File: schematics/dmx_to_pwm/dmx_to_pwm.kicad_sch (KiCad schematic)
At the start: 39 parts, among them J2 DMX-IN, J3 DMX-OUT, Q1 BS170, Q10 BS170, Q11 BS170, Q12 BS170, Q2 BS170, Q3 BS170, Q4 BS170, Q5 BS170, Q6 BS170, Q7 BS170, Q8 BS170, Q9 BS170, U1 SN75176AP, U2 6N137, U3 6N137, U4 SN75176AP

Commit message: updated some components
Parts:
- removed Q1, Q10, Q11, Q12, Q2, Q3, Q4, Q5, Q6, Q7, Q8, Q9: BS170, Package_TO_SOT_THT:TO-92_Inline, symbol Transistor_FET:BS170
- added C3: 10uF, symbol Device:C_Polarized
- added C4: 330nF, symbol Device:C
- added C5, C6: 100nF, symbol Device:C
- added D1, D2: 1N4148, Diode_THT:D_DO-35_SOD27_P7.62mm_Horizontal, symbol Diode:1N4148
- added J4: PJ-031D, PJ031D, symbol PJ-031D:PJ-031D
- added SW2: SW_SPDT, Button_Switch_THT:SW_Slide-03_Wuerth-WS-SLTV_10x2.5x6.4_P2.54mm, symbol Switch:SW_Wuerth_450301014042
- added SW3: SW_Push_DPDT, symbol Switch:SW_Push_DPDT
- added U5: LM7812_TO220, Package_TO_SOT_THT:TO-220-3_Vertical, symbol Regulator_Linear:LM7812_TO220
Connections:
- net GND is gone; now on net DRV1-: A1.29 (GND), A1.4 (GND), C1.2, C2.2, J2.7, J2.8, J3.7, J3.8, R17.2, U1.2 (~{RE}), U1.3 (DE), U1.4 (D), U1.5 (GND), U2.3 (C), U2.5 (GND), U3.3 (C), U3.5 (GND), U4.5 (GND)
- net DATA10: now also R10.1; no longer R4.1
- net DATA11: now also R11.1; no longer R5.1
- net DATA12: now also R12.1; no longer R6.1
- net DATA2: now also R1.1; no longer R8.1
- net DATA3: now also R2.1; no longer R9.1
- net DATA4: now also R3.1; no longer R10.1
- net DATA5: now also R4.1; no longer R11.1
- net DATA6: now also R5.1; no longer R12.1
- net DATA7: now also R6.1; no longer R1.1
- net DATA8: now also R8.1; no longer R2.1
- net DATA9: now also R9.1; no longer R3.1
- net DRV1+: now also R7.2; no longer C1.1, C2.1, R14.1, R16.1, R19.2, U1.8 (VCC), U2.8 (VCC), U3.7 (EN), U3.8 (VCC), U4.2 (~{RE}), U4.3 (DE), U4.8 (VCC)
- net DRV1-: now also C3.2, C4.2, C5.2, C6.1, J4.1, U5.2 (GND)
- net DRV3+: now reaches R2.2
- net DRV11+: now reaches R11.2
- net DRV4+: now reaches R3.2
- net DRV2+: now reaches R1.2
- net VIN: now reaches A1.30 (VIN)
- net VIN: now also C6.2, D1.1 (K), D2.1 (K), SW2.3 (A), SW3.4 (A)
- net DRV12+: now reaches R12.2
- net DRV5+: now reaches R4.2
- net DRV9+: now reaches R9.2
- net at J2.5: now also J2.6, SW3.2 (B)
- net DRV7+: now reaches R6.2
- net DRV10+: now reaches R10.2
- net DRV6+: now reaches R5.2
- net at J3.5: now also J3.6, SW3.5 (B)
- net DRV8+: now reaches R8.2
- new net: C3.1, J4.3
- new net: C4.1, U5.1 (VI)
- new net: C5.1, D2.2 (A), U5.3 (VO)
- new net: SW2.1 (B), SW3.1 (A)
- new net VCC: C1.1, C2.1, R14.1, R16.1, R19.2, U1.8 (VCC), U2.8 (VCC), U3.7 (EN), U3.8 (VCC), U4.2 (~{RE}), U4.3 (DE), U4.8 (VCC)
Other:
- note added: "POE ON/OFF"
- note added: "POE_IN ON/OFF"
- note added: "VOLTAGE REGULATOR ON/OFF"
- moved on the sheet: A1, C1, C2, R13, R14, R15, R16, R17, R19, R7, U1, U2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

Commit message: improved schematics
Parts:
- removed SW3: SW_Push_DPDT, symbol Switch:SW_Push_DPDT
- added SW1: SW_SPDT, Button_Switch_THT:SW_Slide-03_Wuerth-WS-SLTV_10x2.5x6.4_P2.54mm, symbol Switch:SW_Wuerth_450301014042
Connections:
- net VIN: now also SW1.3 (A)
- net at SW2.1 (B): now also J2.5, J2.6
- net at J3.5, J3.6: now also SW1.1 (B)
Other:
- note added: "POE_OUT ON/OFF"
- note removed: "POE ON/OFF"
- moved on the sheet: SW2
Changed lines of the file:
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@@
 	)
 	(junction
-		(at 46.99 48.26)
+		(at 157.48 33.02)
 		(diameter 0)
 		(color 0 0 0 0)
 	)
 	(junction
-		(at 157.48 33.02)
+		(at 46.99 48.26)
 		(diameter 0)
 		(color 0 0 0 0)
@@
 	(wire
 		(pts
-			(xy 46.99 52.07) (xy 46.99 48.26)
-		)
-		(stroke
-			(width 0)
-			(type default)
-		)
-	)
-	(wire
-		(pts
 			(xy 267.97 76.2) (xy 266.7 76.2)
 		)
@@
 	(wire
 		(pts
+			(xy 46.99 48.26) (xy 63.5 48.26)
+		)
+		(stroke
+			(width 0)
+			(type default)
+		)
+	)
+	(wire
+		(pts
 			(xy 104.14 44.45) (xy 104.14 38.1)
 		)
@@
 	(wire
 		(pts
-			(xy 57.15 49.53) (xy 63.5 49.53)
-		)
-		(stroke
-			(width 0)
-			(type default)
-		)
-	)
-	(wire
-		(pts
 			(xy 223.52 91.44) (xy 226.06 91.44)
 		)
@@
 		)
 	)
-	(text "POE ON/OFF"
+	(text "POE_OUT ON/OFF"
 		(exclude_from_sim no)
 		(at 52.07 68.072 0)
@@
 	(text "POE_IN ON/OFF"
 		(exclude_from_sim no)
-		(at 69.342 55.88 0)
+		(at 69.342 54.102 0)
 		(effects
 			(font
@@
 		)
 	)
-	(global_label "VIN"
-		(shape input)
-		(at 57.15 59.69 0)
-		(fields_autoplaced yes)
-		(effects
-			(font
-				(size 1.27 1.27)
-			)
-			(justify left)
-		)
-		(property "Intersheetrefs" "${INTERSHEET_REFS}"
-			(at 63.1591 59.69 0)
-			(effects
-				(font
-					(size 1.27 1.27)
-				)
-				(justify left)
-				(hide yes)
-			)
-		)
-	)
 	(global_label "DATA11"
 		(shape input)
@@
 		)
 	)
+	(global_label "VIN"
+		(shape input)
+		(at 57.15 59.69 0)
+		(fields_autoplaced yes)
+		(effects
+			(font
+				(size 1.27 1.27)
+			)
+			(justify left)
+		)
+		(property "Intersheetrefs" "${INTERSHEET_REFS}"
+			(at 63.1591 59.69 0)
+			(effects
+				(font
+					(size 1.27 1.27)
+				)
+				(justify left)
+				(hide yes)
+			)
+		)
+	)
 	(global_label "DRV6-"
 		(shape input)
@@
 	(global_label "VIN"
 		(shape input)
-		(at 73.66 46.99 0)
+		(at 73.66 45.72 0)
 		(fields_autoplaced yes)
 		(effects
@@
 		)
 		(property "Intersheetrefs" "${INTERSHEET_REFS}"
-			(at 79.6691 46.99 0)
+			(at 79.6691 45.72 0)
 			(effects
 				(font
@@
 	(symbol
 		(lib_id "Switch:SW_Wuerth_450301014042")
-		(at 68.58 49.53 0)
+		(at 68.58 48.26 0)
 		(unit 1)
 		(exclude_from_sim no)
@@
 		(fields_autoplaced yes)
 		(property "Reference" "SW2"
-			(at 68.58 40.64 0)
+			(at 68.58 39.37 0)
 			(effects
 				(font
@@
 		)
 		(property "Value" "SW_SPDT"
-			(at 68.58 43.18 0)
+			(at 68.58 41.91 0)
 			(effects
 				(font
@@
 		)
 		(property "Footprint" "Button_Switch_THT:SW_Slide-03_Wuerth-WS-SLTV_10x2.5x6.4_P2.54mm"
-			(at 68.58 59.69 0)
+			(at 68.58 58.42 0)
 			(effects
 				(font
@@
 		)
 		(property "Datasheet" "https://www.we-online.com/components/products/datasheet/450301014042.pdf"
-			(at 68.58 57.15 0)
+			(at 68.58 55.88 0)
 			(effects
 				(font
@@
 		)
 		(property "Description" "Switch slide, single pole double throw"
-			(at 68.58 49.53 0)
+			(at 68.58 48.26 0)
 			(effects
 				(font
@@
 	)
 	(symbol
+		(lib_id "Switch:SW_Wuerth_450301014042")
+		(at 52.07 62.23 0)
+		(unit 1)
+		(exclude_from_sim no)
+		(in_bom yes)
+		(on_board yes)
+		(dnp no)
+		(fields_autoplaced yes)
+		(property "Reference" "SW1"
+			(at 52.07 53.34 0)
+			(effects
+				(font
+					(size 1.27 1.27)
+				)
+			)
+		)
+		(property "Value" "SW_SPDT"
+			(at 52.07 55.88 0)
+			(effects
+				(font
+					(size 1.27 1.27)
+				)
+			)
+		)
+		(property "Footprint" "Button_Switch_THT:SW_Slide-03_Wuerth-WS-SLTV_10x2.5x6.4_P2.54mm"
+			(at 52.07 72.39 0)
+			(effects
+				(font
+					(size 1.27 1.27)
+				)
+				(hide yes)
+			)
+		)
+		(property "Datasheet" "https://www.we-online.com/components/products/datasheet/450301014042.pdf"
+			(at 52.07 69.85 0)
+			(effects
+				(font
+					(size 1.27 1.27)
+				)
+				(hide yes)
+			)
+		)
+		(property "Description" "Switch slide, single pole double throw"
+			(at 52.07 62.23 0)
+			(effects
+				(font
+					(size 1.27 1.27)
+				)
+				(hide yes)
+			)
+		)
+		(pin "1"
+		)
+		(pin "2"
+		)
+		(pin "3"
+		)
+		(instances
+			(project "dmx_to_pwm"
+				(path "/fe39f169-33b8-46fd-886b-c754b4eb741b"
+					(reference "SW1")
+					(unit 1)
+				)
+			)
+		)
+	)
+	(symbol
 		(lib_id "Device:R_US")
 		(at 219.71 24.13 90)
@@
 					(unit 1)
 				)
-			)
-		)
-	)
-	(symbol
-		(lib_id "Switch:SW_Push_DPDT")
-		(at 52.07 57.15 0)
-		(unit 1)
-		(exclude_from_sim no)
-		(in_bom yes)
-		(on_board yes)
-		(dnp no)
-		(property "Reference" "SW3"
-			(at 52.07 43.18 0)
-			(effects
-				(font
-					(size 1.27 1.27)
-				)
-			)
-		)
-		(property "Value" "SW_Push_DPDT"
-			(at 55.626 45.72 0)
-			(effects
-				(font
-					(size 1.27 1.27)
-				)
-			)
-		)
-		(property "Footprint" ""
-			(at 52.07 52.07 0)
-			(effects
-				(font
-					(size 1.27 1.27)
-				)
-				(hide yes)
-			)
-		)
-		(property "Datasheet" "~"
-			(at 52.07 52.07 0)
-			(effects
-				(font
-					(size 1.27 1.27)
-				)
-				(hide yes)
-			)
-		)
-		(property "Description" "Momentary Switch, dual pole double throw"
-			(at 52.07 57.15 0)
-			(effects
-				(font
-					(size 1.27 1.27)
-				)
-				(hide yes)
-			)
-		)
-		(pin "2"
-		)
-		(pin "1"
-		)
-		(pin "5"
-		)
-		(pin "3"
-		)
-		(pin "4"
-		)
-		(pin "6"
-		)
-		(instances
-			(project "dmx_to_pwm"
-				(path "/fe39f169-33b8-46fd-886b-c754b4eb741b"
-					(reference "SW3")
-					(unit 1)
-				)

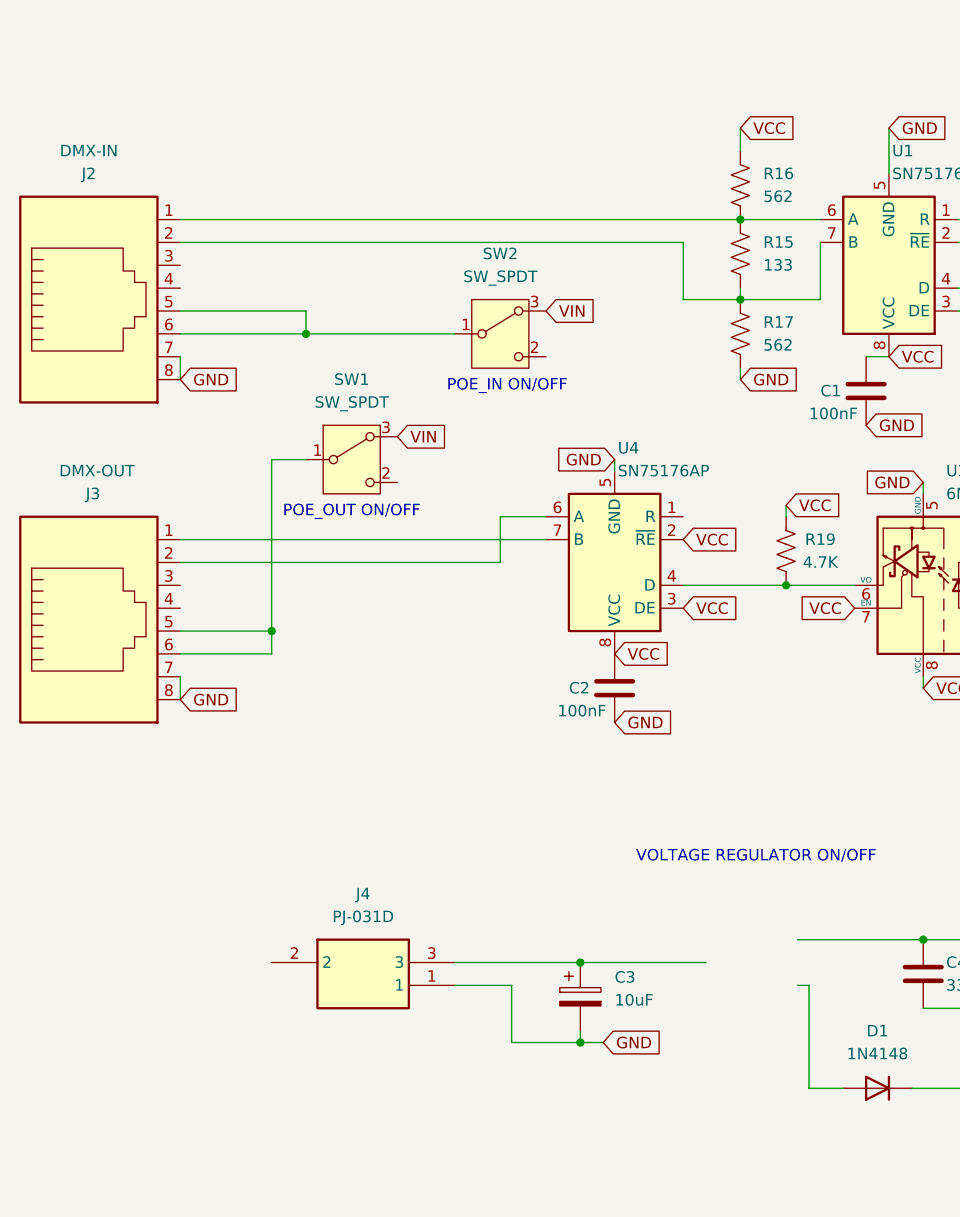
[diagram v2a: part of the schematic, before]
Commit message: #5 improved schematics
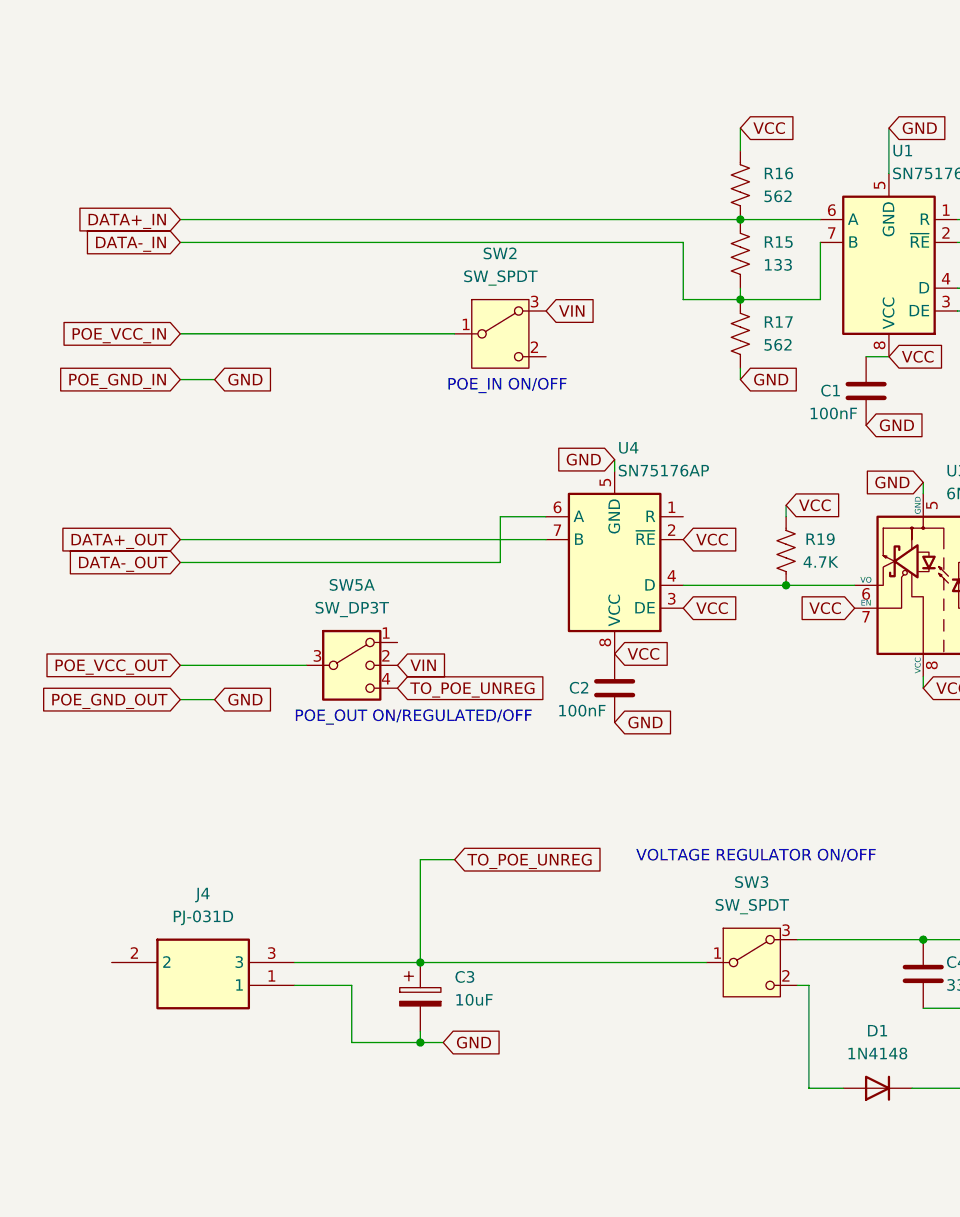
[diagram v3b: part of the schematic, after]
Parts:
- removed J2: DMX-IN, symbol Connector:RJ45
- removed J3: DMX-OUT, symbol Connector:RJ45
- removed SW1: SW_SPDT, Button_Switch_THT:SW_Slide-03_Wuerth-WS-SLTV_10x2.5x6.4_P2.54mm, symbol Switch:SW_Wuerth_450301014042
- added SW3: SW_SPDT, Button_Switch_THT:SW_Slide-03_Wuerth-WS-SLTV_10x2.5x6.4_P2.54mm, symbol Switch:SW_Wuerth_450301014042
- added SW5: SW_DP3T, symbol Switch:SW_DP3T
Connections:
- net VIN: now also SW5.2
- net TO_POE_UNREG: now reaches C3.1, J4.3
- net TO_POE_UNREG: now also SW3.1 (B), SW5.4
- net DATA+_IN: now reaches R15.1, R16.2, U1.6 (A)
- net DATA-_IN: now reaches R15.2, R17.1, U1.7 (B)
- net at C4.1, U5.1 (VI): now also SW3.3 (A)
- net at D1.2 (A): now also SW3.2 (C)
- net POE_VCC_IN: now reaches SW2.1 (B)
- net DATA+_OUT: now reaches U4.7 (B)
- net DATA-_OUT: now reaches U4.6 (A)
- new net POE_VCC_OUT: SW5.3
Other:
- note added: "POE_OUT ON/REGULATED/OFF"
- note removed: "POE_OUT ON/OFF"
- moved on the sheet: C3, J4

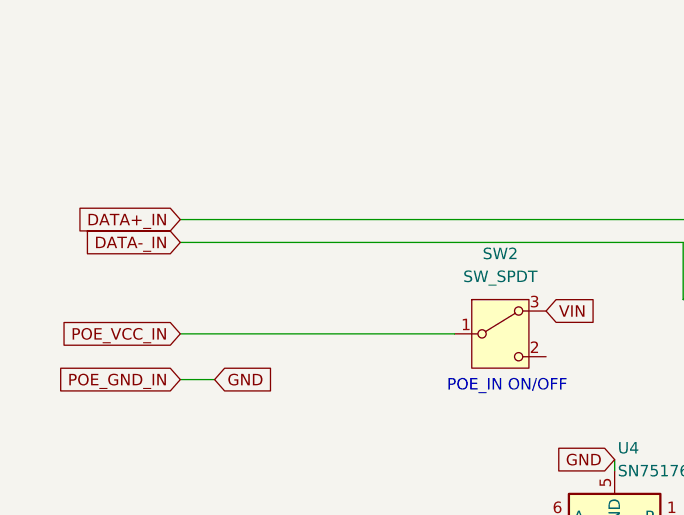
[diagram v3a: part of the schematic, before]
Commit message: added some prototype info to the schematics
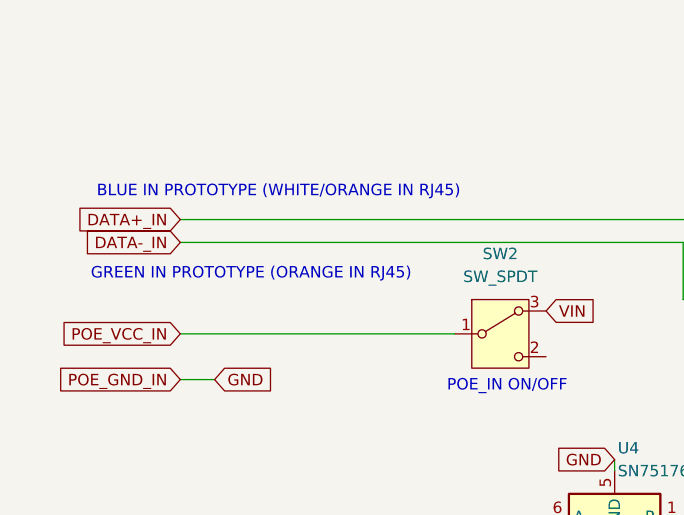
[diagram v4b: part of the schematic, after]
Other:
- note added: "BLUE IN PROTOTYPE (WHITE/ORANGE IN RJ45)"
- note added: "GREEN IN PROTOTYPE (ORANGE IN RJ45)"
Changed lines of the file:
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@@
+		)
+	)
+	(text "GREEN IN PROTOTYPE (ORANGE IN RJ45)"
+		(exclude_from_sim no)
+		(at 40.894 41.656 0)
+		(effects
+			(font
+				(size 1.27 1.27)
+			)
+		)
+	)
+	(text "BLUE IN PROTOTYPE (WHITE/ORANGE IN RJ45)"
+		(exclude_from_sim no)
+		(at 43.942 32.512 0)
+		(effects
+			(font
+				(size 1.27 1.27)
+			)
 		)
 	)

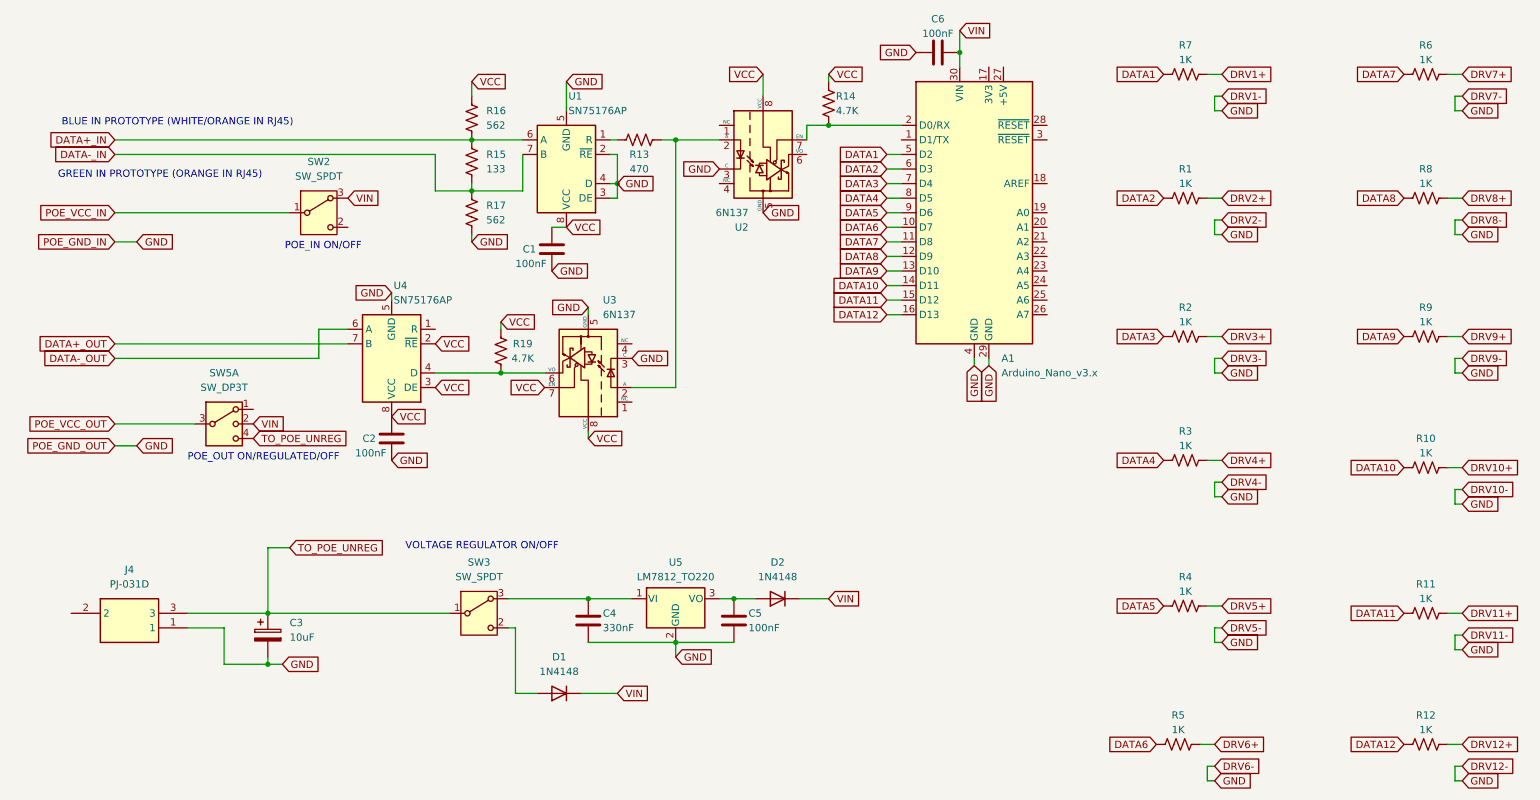
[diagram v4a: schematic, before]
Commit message: updated schematics, added laser module blender file
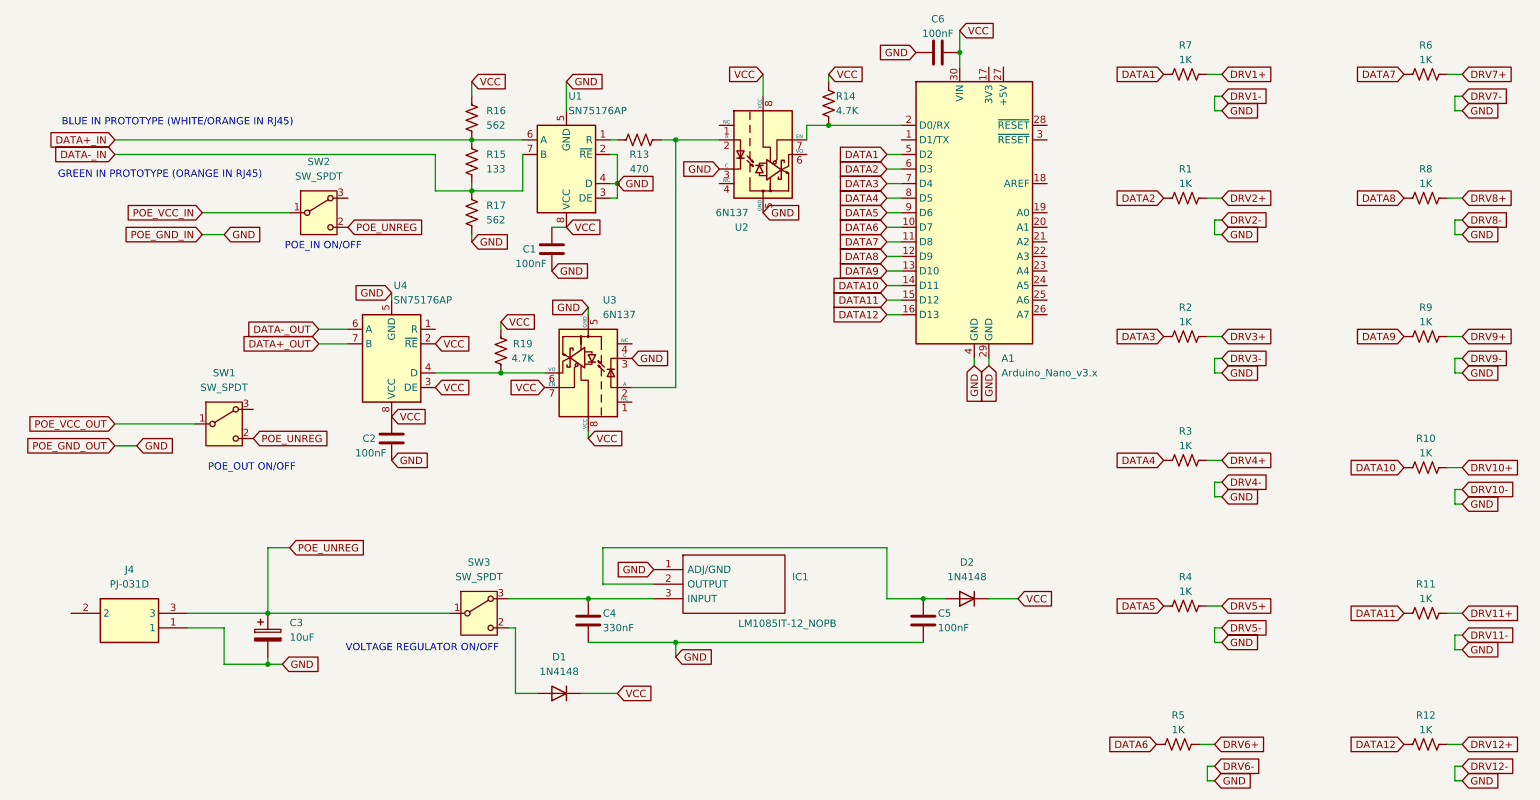
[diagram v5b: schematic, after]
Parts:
- removed SW5: SW_DP3T, symbol Switch:SW_DP3T
- removed U5: LM7812_TO220, Package_TO_SOT_THT:TO-220-3_Vertical, symbol Regulator_Linear:LM7812_TO220
- added IC1: LM1085IT-12_NOPB, Lasers:TO254P470X1028X1955-3P, symbol lasers_rgb:LM1085IT-12_NOPB
- added SW1: SW_SPDT, Button_Switch_THT:SW_Slide-03_Wuerth-WS-SLTV_10x2.5x6.4_P2.54mm, symbol Switch:SW_Wuerth_450301014042
- C1, C2, C5: footprint (none) -> Capacitor_THT:C_Disc_D3.0mm_W2.0mm_P2.50mm
- C3, C4: footprint (none) -> Capacitor_THT:CP_Radial_Tantal_D5.5mm_P2.50mm
- R1, R10, R11, R12, R13, R14, R15, R16, R17, R19, R2, R3, R4, R5, R6, R7, R8, R9: footprint (none) -> Resistor_THT:R_Axial_DIN0204_L3.6mm_D1.6mm_P7.62mm_Horizontal
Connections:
- net TO_POE_UNREG is gone; now on net POE_UNREG: C3.1, J4.3, SW3.1 (B)
- net DRV1-: now also IC1.1 (ADJ/GND)
- net POE_VCC_OUT: now also SW1.1 (B)
- net VCC: now also A1.30 (VIN), C6.2, D1.1 (K), D2.1 (K)
- net at C4.1, SW3.3 (A): now also IC1.3 (INPUT)
- net at C5.1, D2.2 (A): now also IC1.2 (OUTPUT)
- net POE_UNREG: now reaches SW2.2 (C)
- net POE_UNREG: now also SW1.2 (C)
- removed net VIN: A1.30 (VIN), C6.2, D1.1 (K), D2.1 (K), SW2.3 (A)
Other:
- note added: "POE_OUT ON/OFF"
- note removed: "POE_OUT ON/REGULATED/OFF"
- moved on the sheet: C5, D2
